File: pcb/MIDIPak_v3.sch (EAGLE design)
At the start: 38 parts, among them IC1 74LS133N, IC3 74LS138N, IC4 68B50, IC5 74LS04N, IC6 74*161, X1 MIDI_IN, X2 MIDI_THRU, X3 MIDI_OUT, X4 EXPANSION_PORT_COCO

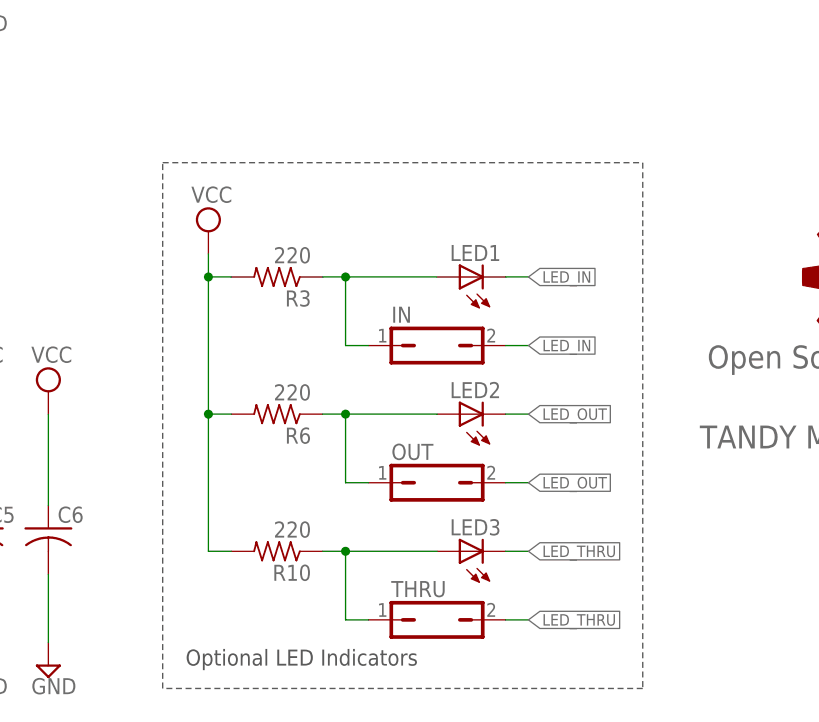
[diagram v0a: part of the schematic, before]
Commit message: Fixed polarity issues with LED signals
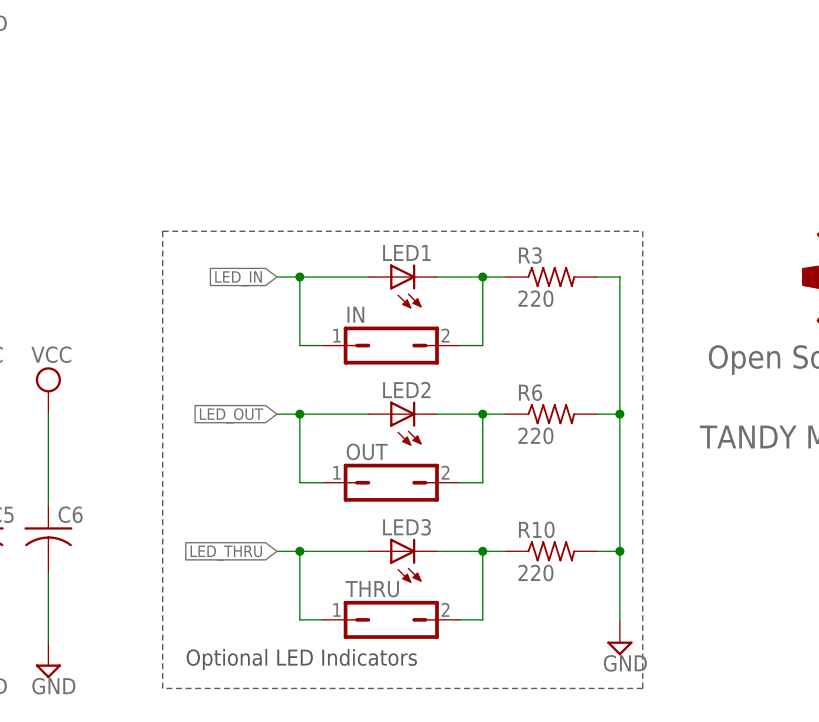
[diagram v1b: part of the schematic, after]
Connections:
- removed net N$19: LED3.A, R10.1, THRU.1
- new net N$17: LED2.C, OUT.2, R6.1
- net GND: now also R10.2, R3.2, R6.2
- net LED_IN: now also IN.1, LED1.A; no longer IN.2, LED1.C
- net LED_OUT: now also LED2.A, OUT.1; no longer LED2.C, OUT.2
- net LED_THRU: now also LED3.A, THRU.1; no longer LED3.C, THRU.2
- net N$12: now also IN.2, LED1.C; no longer IN.1, LED1.A
- net N$18: now also LED3.C, R10.1, THRU.2; no longer LED2.A, OUT.1, R6.1
- net VCC: no longer R10.2, R3.2, R6.2
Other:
- moved on the sheet: IN, LED1, LED2, LED3, OUT, R10, R3, R6, THRU
